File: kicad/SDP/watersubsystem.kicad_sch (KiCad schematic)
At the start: 6 parts

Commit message: Updated schematics
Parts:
- removed D?: D_Small, symbol Device:D_Small
- removed J?: Conn_01x02, symbol Connector_Generic:Conn_01x02
- removed K?: SANYOU_SRD_Form_C, Relay_THT:Relay_SPDT_SANYOU_SRD_Series_Form_C, symbol Relay:SANYOU_SRD_Form_C
- removed Q?: S8050, Package_TO_SOT_THT:TO-92_Inline, symbol Transistor_BJT:S8050
- removed R?: 10k, symbol Device:R_Small
- removed R?: 330, symbol Device:R_Small
- added D?: D_Small, symbol Device:D_Small
- added J?: Conn_01x02, symbol Connector_Generic:Conn_01x02
- added J?: Conn_01x07, symbol Connector_Generic:Conn_01x07
- added K?: SANYOU_SRD_Form_C, Relay_THT:Relay_SPDT_SANYOU_SRD_Series_Form_C, symbol Relay:SANYOU_SRD_Form_C
- added Q?: S8050, Package_TO_SOT_THT:TO-92_Inline, symbol Transistor_BJT:S8050
- added R?: 330, symbol Device:R_Small
- added R?: 10k, symbol Device:R_Small
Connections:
- net +3V3: now also D?.1 (K), J?.2 (Pin_2), K?.1
- net GND: now also J?.3 (Pin_3), K?.5, Q?.1 (E), R?.2
- net VAC: now also J?.1 (Pin_1)
- new net: Q?.2 (B), R?.1, R?.2
- new net: D?.2 (A), K?.3, Q?.3 (C)
- new net: J?.2 (Pin_2), K?.2
- new net P56_SDA1: J?.4 (Pin_4)
- new net P57_SCL1: J?.5 (Pin_5)
- new net P7_HTR_RLY: R?.1
- new net Pxx_CE: J?.6 (Pin_6)
- no-connect marks 0 -> 2

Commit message: Updated schematics
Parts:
- added C?: 470u, symbol Device:C_Small
- added D?: 1N4007, Diode_THT:D_DO-41_SOD81_P10.16mm_Horizontal, symbol Diode:1N4007
- added J?: Conn_01x02, symbol Connector_Generic:Conn_01x02
- added J?: Conn_01x03, symbol Connector_Generic:Conn_01x03
- added J?: Conn_01x07, symbol Connector_Generic:Conn_01x07
- added Q?: IRLZ44N, Package_TO_SOT_THT:TO-220-3_Vertical, symbol Transistor_FET:IRLZ44N
- added R?: 10k, symbol Device:R_Small
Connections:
- net +3V3: now also J?.2 (Pin_2), J?.3 (Pin_3)
- net GND: now also J?.1 (Pin_1), C?.2, J?.1 (Pin_1), J?.3 (Pin_3), Q?.3 (S), R?.2; no longer K?.5
- net P56_SDA1: now also J?.4 (Pin_4)
- net P57_SCL1: now also J?.5 (Pin_5)
- net VAC: now also K?.2; no longer J?.1 (Pin_1)
- net at J?.2 (Pin_2): now also K?.5; no longer K?.2
- net Pxx_CE renamed P95_TOF1_CE
- new net: D?.2 (A), J?.1 (Pin_1), Q?.2 (D)
- new net +12V: C?.1, D?.1 (K), J?.2 (Pin_2)
- new net P87_MTR1: Q?.1 (G), R?.1
- new net P91_TEMP: J?.2 (Pin_2)
- new net P96_TOF2_CE: J?.6 (Pin_6)
- no-connect marks 2 -> 4
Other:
- moved on the sheet: D?, J?, K?, Q?, R?

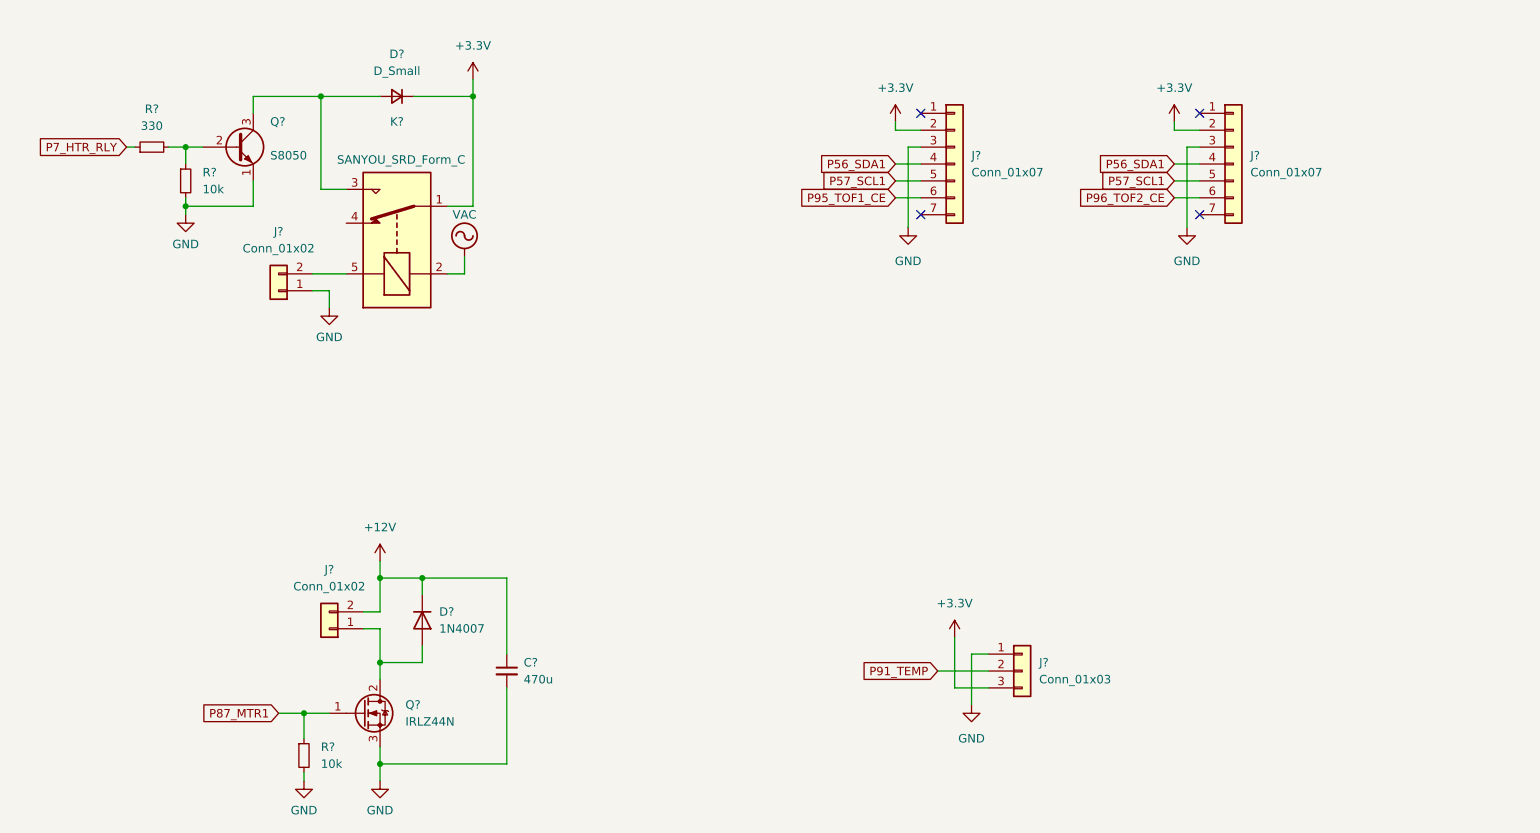
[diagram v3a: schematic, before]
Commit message: Added GPIO headers, separated power PCB
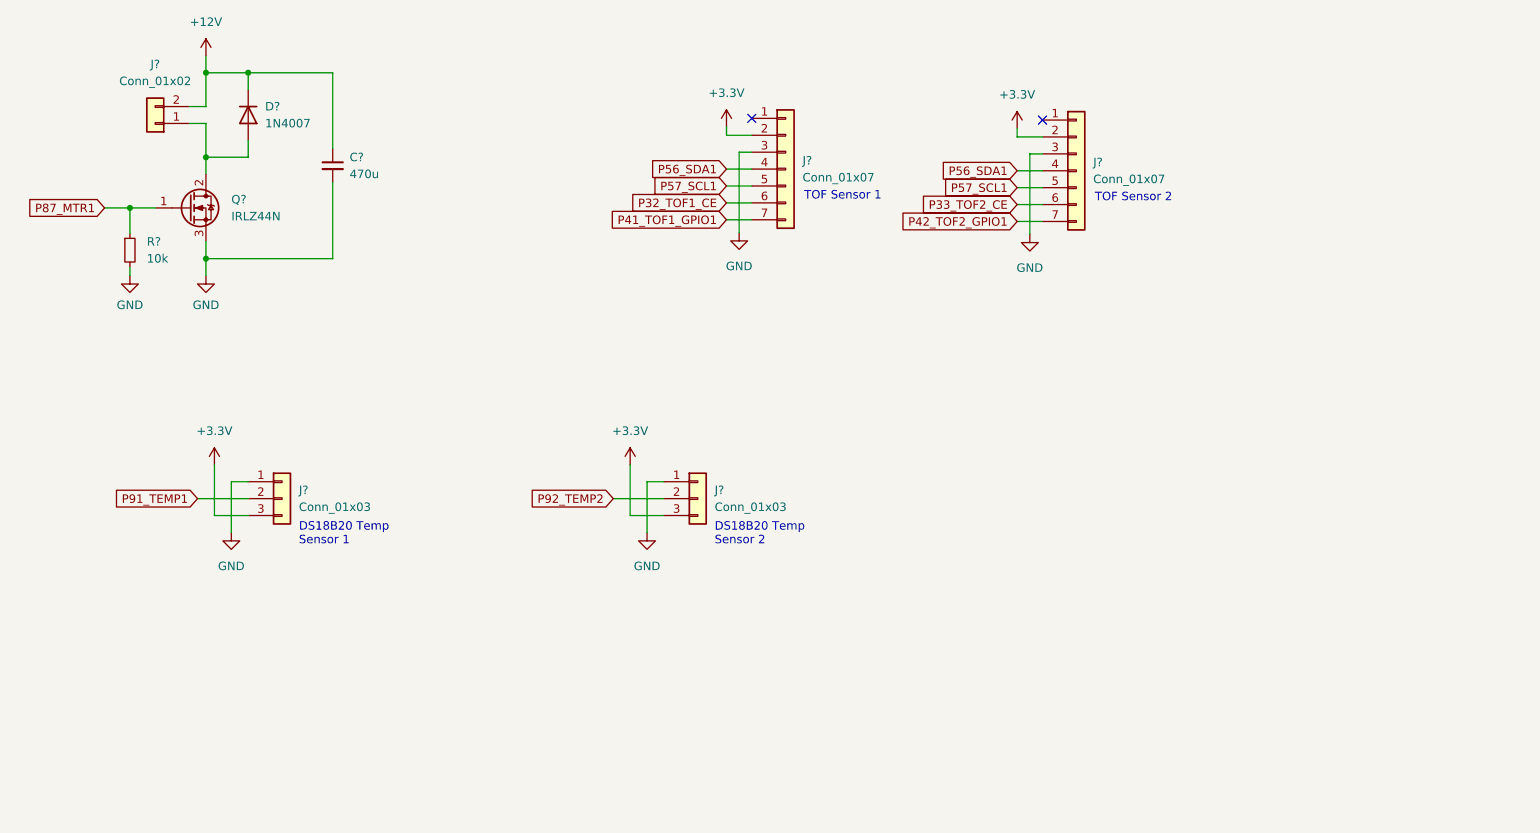
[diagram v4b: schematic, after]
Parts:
- removed D?: D_Small, symbol Device:D_Small
- removed J?: Conn_01x02, symbol Connector_Generic:Conn_01x02
- removed K?: SANYOU_SRD_Form_C, Relay_THT:Relay_SPDT_SANYOU_SRD_Series_Form_C, symbol Relay:SANYOU_SRD_Form_C
- removed Q?: S8050, Package_TO_SOT_THT:TO-92_Inline, symbol Transistor_BJT:S8050
- removed R?: 330, symbol Device:R_Small
- removed R?: 10k, symbol Device:R_Small
- added J?: Conn_01x03, symbol Connector_Generic:Conn_01x03
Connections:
- net +3V3: now also J?.3 (Pin_3)
- net GND: now also J?.1 (Pin_1)
- net P42_TOF2_GPIO1: now reaches J?.7 (Pin_7)
- net P41_TOF1_GPIO1: now reaches J?.7 (Pin_7)
- net P91_TEMP renamed P92_TEMP2
- net P95_TOF1_CE renamed P32_TOF1_CE
- net P96_TOF2_CE renamed P33_TOF2_CE
- new net P91_TEMP1: J?.2 (Pin_2)
- no-connect marks 4 -> 2
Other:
- note added: "DS18B20 Temp Sensor 1"
- note added: "DS18B20 Temp Sensor 2"
- note added: "TOF Sensor 1"
- note added: "TOF Sensor 2"
- moved on the sheet: C?, D?, J?, Q?, R?

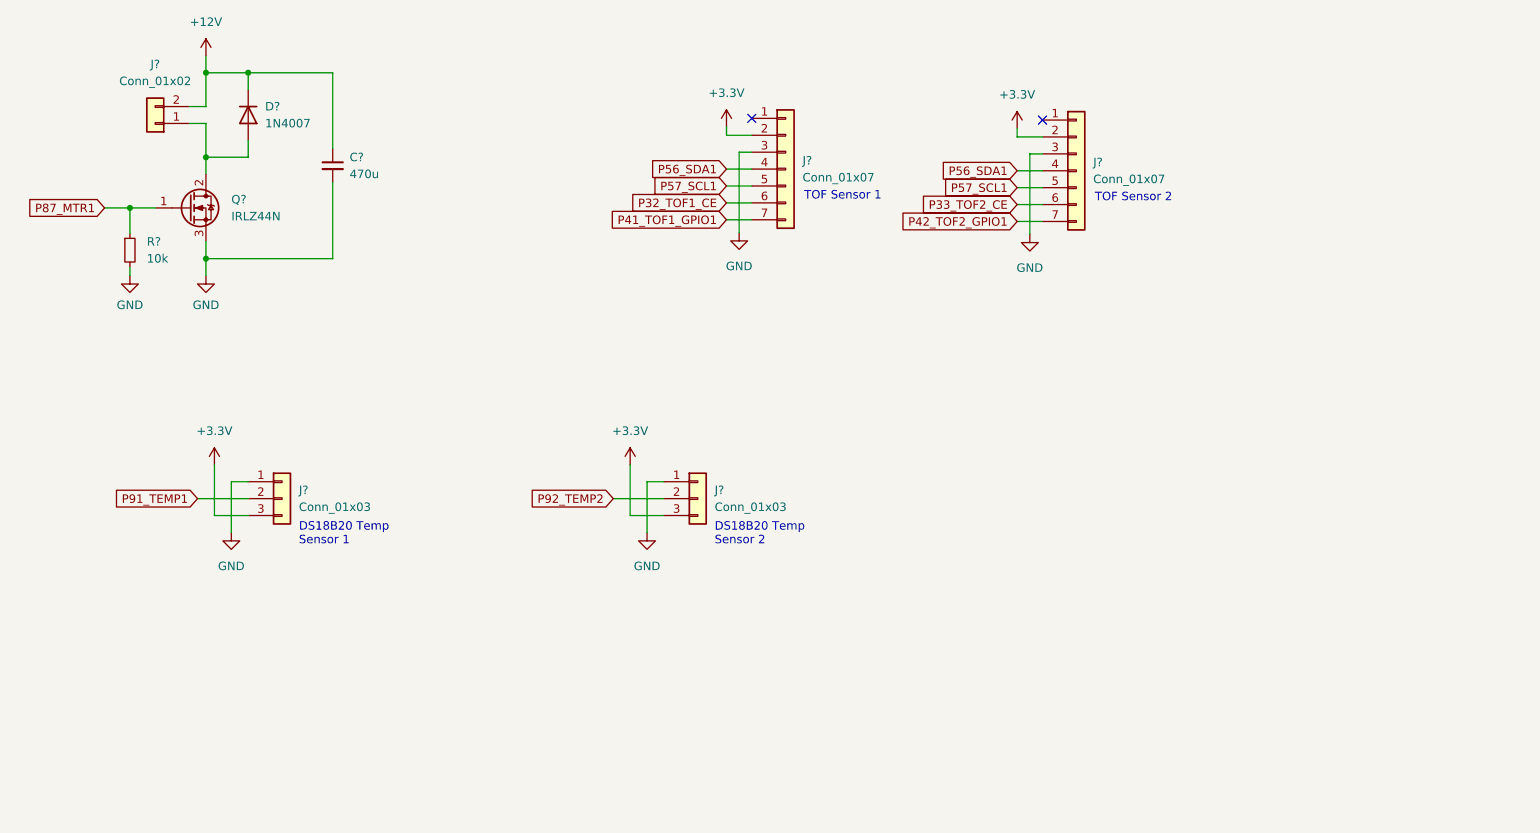
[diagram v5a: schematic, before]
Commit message: Added footprints
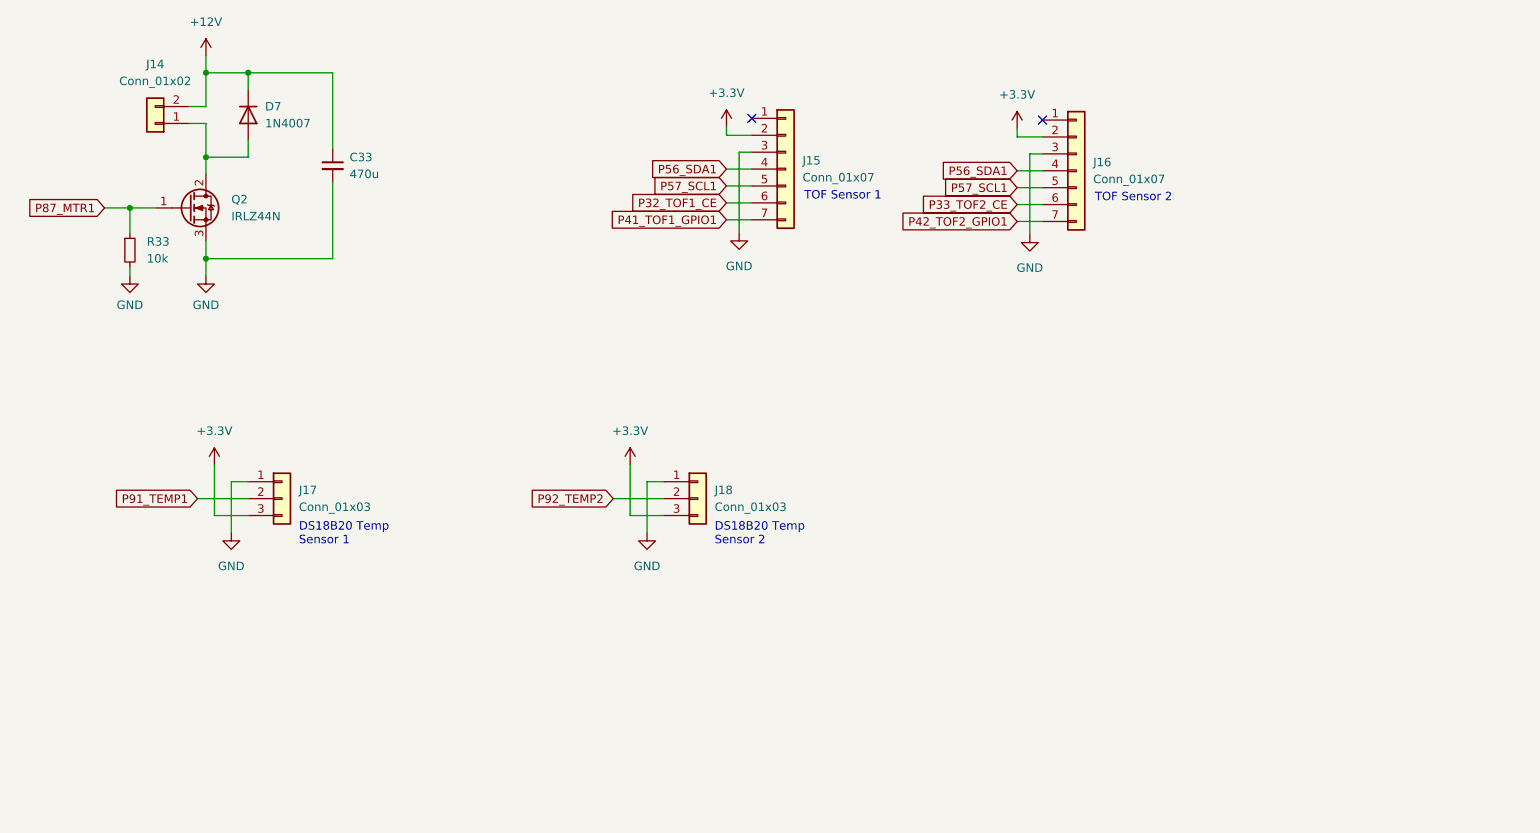
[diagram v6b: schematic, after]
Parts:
- gave numbers to parts that had none: 9
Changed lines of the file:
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@@
   (symbol (lib_id "Transistor_FET:IRLZ44N") (at 42.418 49.784 0) (unit 1)
     (in_bom yes) (on_board yes) (fields_autoplaced)
-    (property "Reference" "Q?" (id 0) (at 48.768 48.5139 0)
+    (property "Reference" "Q2" (id 0) (at 48.768 48.5139 0)
       (effects (font (size 1.27 1.27)) (justify left))
     )
@@
   (symbol (lib_id "Diode:1N4007") (at 51.308 35.814 270) (unit 1)
     (in_bom yes) (on_board yes) (fields_autoplaced)
-    (property "Reference" "D?" (id 0) (at 53.848 34.5439 90)
+    (property "Reference" "D7" (id 0) (at 53.848 34.5439 90)
       (effects (font (size 1.27 1.27)) (justify left))
     )
@@
   (symbol (lib_id "Device:C_Small") (at 64.008 43.434 0) (unit 1)
     (in_bom yes) (on_board yes) (fields_autoplaced)
-    (property "Reference" "C?" (id 0) (at 66.548 42.1702 0)
+    (property "Reference" "C33" (id 0) (at 66.548 42.1702 0)
       (effects (font (size 1.27 1.27)) (justify left))
     )
@@
   (symbol (lib_id "Connector_Generic:Conn_01x02") (at 37.338 37.084 180) (unit 1)
     (in_bom yes) (on_board yes) (fields_autoplaced)
-    (property "Reference" "J?" (id 0) (at 37.338 28.194 0))
+    (property "Reference" "J14" (id 0) (at 37.338 28.194 0))
     (property "Value" "Conn_01x02" (id 1) (at 37.338 30.734 0))
     (property "Footprint" "" (id 2) (at 37.338 37.084 0)
@@
   (symbol (lib_id "Connector_Generic:Conn_01x03") (at 118.872 93.472 0) (unit 1)
     (in_bom yes) (on_board yes) (fields_autoplaced)
-    (property "Reference" "J?" (id 0) (at 121.412 92.2019 0)
+    (property "Reference" "J18" (id 0) (at 121.412 92.2019 0)
       (effects (font (size 1.27 1.27)) (justify left))
     )
@@
   (symbol (lib_id "Connector_Generic:Conn_01x07") (at 175.768 44.196 0) (unit 1)
     (in_bom yes) (on_board yes) (fields_autoplaced)
-    (property "Reference" "J?" (id 0) (at 178.308 42.9259 0)
+    (property "Reference" "J16" (id 0) (at 178.308 42.9259 0)
       (effects (font (size 1.27 1.27)) (justify left))
     )
@@
   (symbol (lib_id "Connector_Generic:Conn_01x07") (at 132.08 43.942 0) (unit 1)
     (in_bom yes) (on_board yes) (fields_autoplaced)
-    (property "Reference" "J?" (id 0) (at 134.62 42.6719 0)
+    (property "Reference" "J15" (id 0) (at 134.62 42.6719 0)
       (effects (font (size 1.27 1.27)) (justify left))
     )
@@
   (symbol (lib_id "Device:R_Small") (at 33.528 56.134 0) (unit 1)
     (in_bom yes) (on_board yes) (fields_autoplaced)
-    (property "Reference" "R?" (id 0) (at 36.068 54.8639 0)
+    (property "Reference" "R33" (id 0) (at 36.068 54.8639 0)
       (effects (font (size 1.27 1.27)) (justify left))
     )
@@
   (symbol (lib_id "Connector_Generic:Conn_01x03") (at 56.388 93.472 0) (unit 1)
     (in_bom yes) (on_board yes) (fields_autoplaced)
-    (property "Reference" "J?" (id 0) (at 58.928 92.2019 0)
-      (effects (font (size 1.27 1.27)) (justify left))
-    )
+    (property "Reference" "J17" (id 0) (at 58.928 92.2019 0)
+      (effects (font (size 1.27 1.27)) (justify left))
+    )

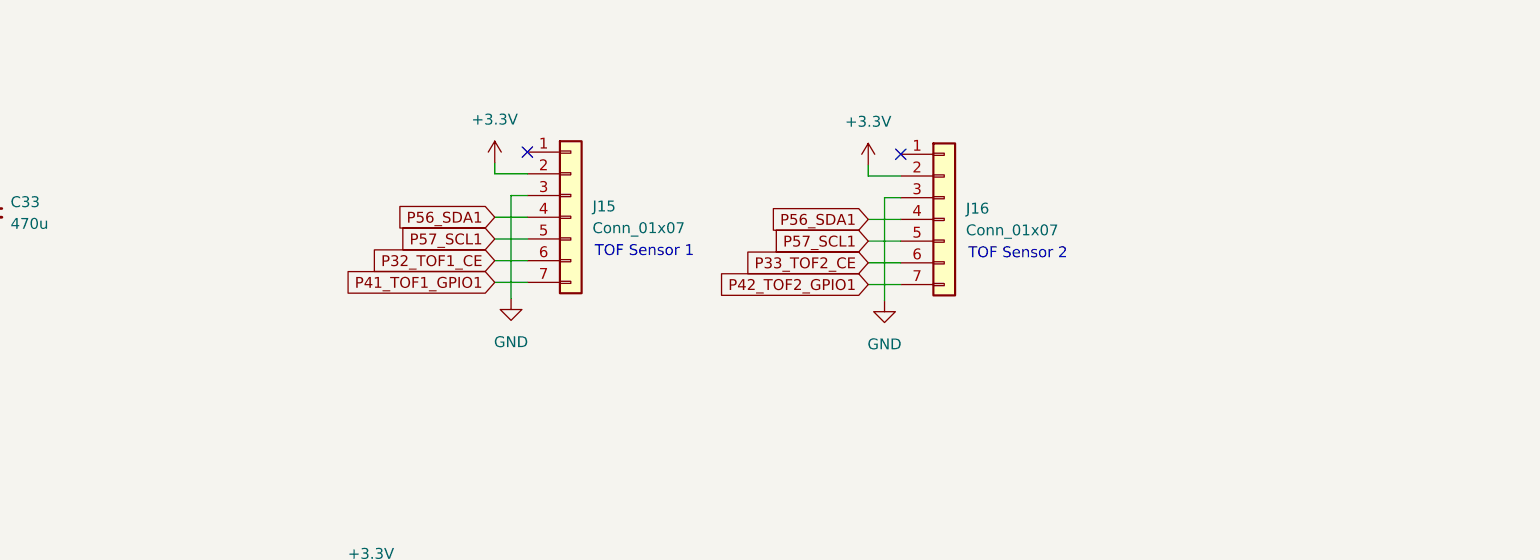
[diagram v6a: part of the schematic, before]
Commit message: Added footprints
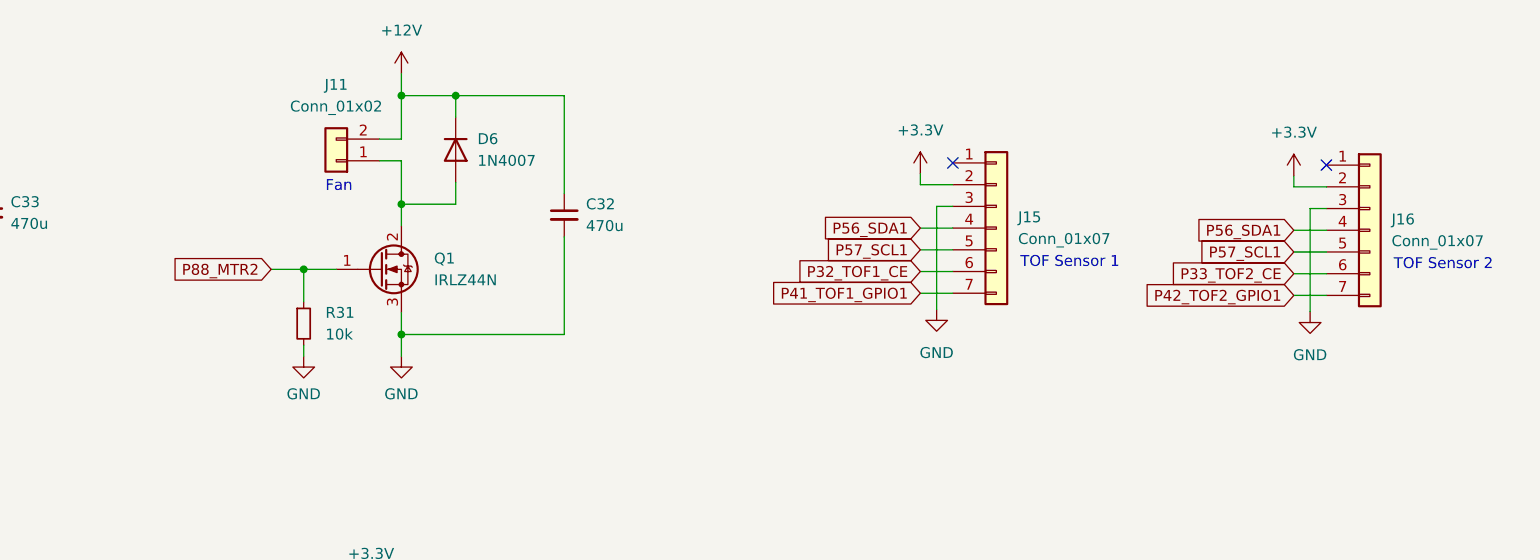
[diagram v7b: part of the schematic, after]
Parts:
- added C32: 470u, symbol Device:C_Small
- added D6: 1N4007, Diode_THT:D_DO-41_SOD81_P10.16mm_Horizontal, symbol Diode:1N4007
- added J11: Conn_01x02, symbol Connector_Generic:Conn_01x02
- added Q1: IRLZ44N, Package_TO_SOT_THT:TO-220-3_Vertical, symbol Transistor_FET:IRLZ44N
- added R31: 10k, Resistor_SMD:R_0805_2012Metric, symbol Device:R_Small
- R33: footprint (none) -> Resistor_SMD:R_0805_2012Metric
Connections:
- net +12V: now also C32.1, D6.1 (K), J11.2 (Pin_2)
- net GND: now also C32.2, Q1.3 (S), R31.2
- new net: D6.2 (A), J11.1 (Pin_1), Q1.2 (D)
- new net P88_MTR2: Q1.1 (G), R31.1
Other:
- note added: "Fan"
- moved on the sheet: J15, J16
